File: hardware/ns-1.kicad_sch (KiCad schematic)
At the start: 66 parts, among them J6 Conn_01x11, J7 USB_C_Receptacle_USB2.0_16P, SW1 SW_Push_45deg, SW10 SW_Push_45deg, SW11 SW_Push_45deg, SW12 SW_Push_45deg, SW13 SW_Push_45deg, SW14 SW_Push_45deg, SW15 SW_Push_45deg, SW16 SW_Push_45deg, SW17 SW_Push_45deg, SW18 SW_Push_45deg, SW19 SW_Push_45deg, SW2 RotaryEncoder_Switch_MP, SW20 SW_Push, SW3 SW_Push_45deg, SW4 SW_Push_45deg, SW5 RotaryEncoder_Switch_MP, SW6 SW_Push_45deg, SW7 RotaryEncoder_Switch_MP, SW8 SW_Push_45deg, SW9 SW_Push_45deg, U1 Teensy4.1

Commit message: start respin to stm32h7
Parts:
- removed U1: Teensy4.1, footprints:Teensy41, symbol teensy:Teensy4.1
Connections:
- no-connect marks 27 -> 5
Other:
- added sheet STM32H7 (stm32h7.kicad_sch)
- added sheet teensy (teensy.kicad_sch)
- note added: "FerretCode"
- moved on the sheet: C2, C3, C4, C6, C8, R4, R5, R6, R7, R8, RV1, RV2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

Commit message: continue h7 revision
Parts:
- added R11, R12: 4.7k, symbol Device:R_Small_US
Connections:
- net +3.3V: now also R11.1, R12.1
- net SCL: now also R11.2
- net SDA: now also R12.2
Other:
- sheet Teensy Audio Shield renamed SGTL5000
- sheet SGTL5000: file teensy_audio_shield.kicad_sch -> sgtl5000.kicad_sch
- sheet SGTL5000 ports: added I2S_DIN, I2S_DOUT, I2S_LRCLK, I2S_SCLK, SYS_MCLK; removed BCLK, DIN, DOUT, LRCLK, MCLK
- sheet STM32H7 ports: added I2S_DIN, I2S_DOUT, I2S_LRCLK, I2S_SCLK, SCL, SDA, SYS_MCLK; removed none

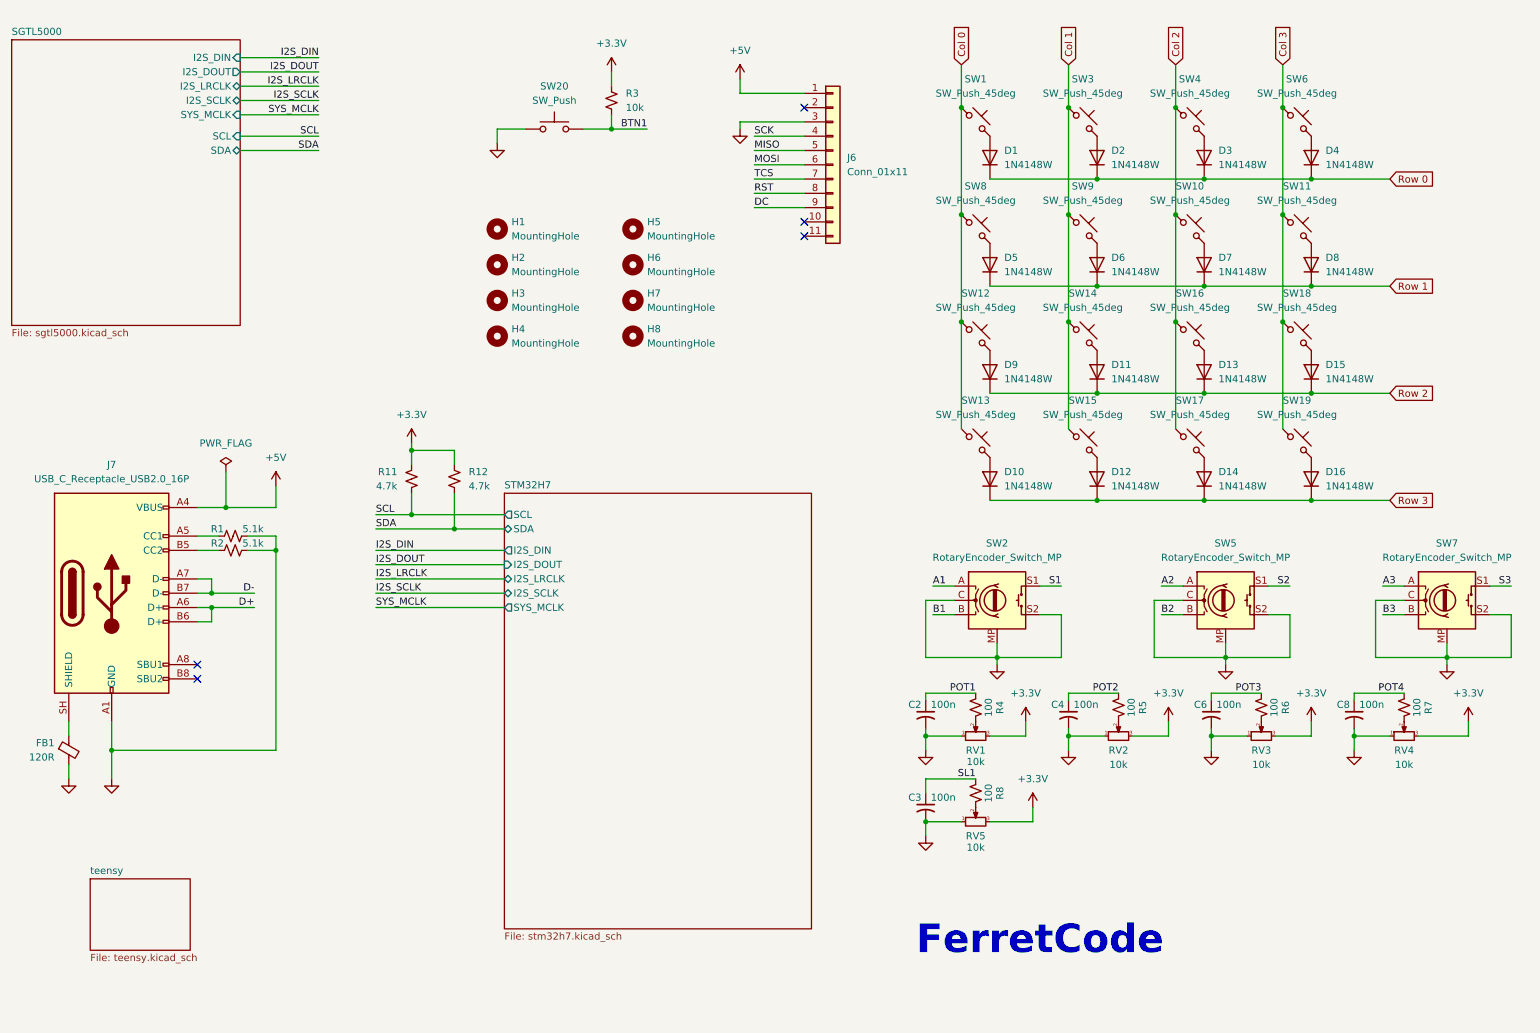
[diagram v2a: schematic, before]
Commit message: reorganize and finish codec / power
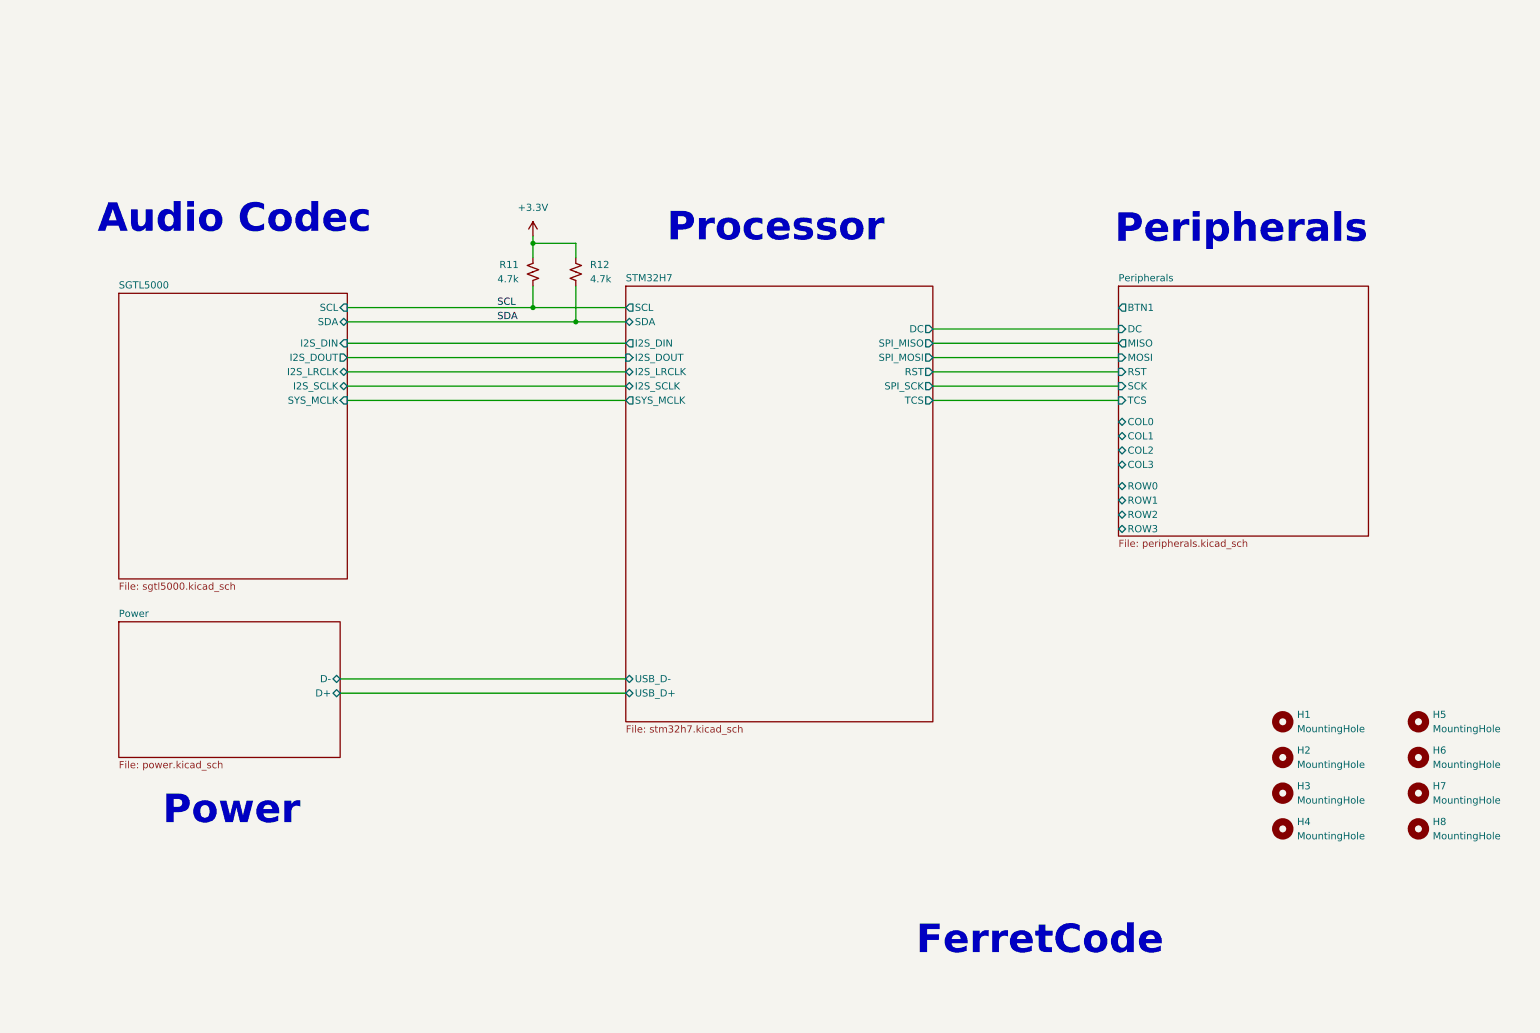
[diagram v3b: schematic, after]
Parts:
- removed C2, C3, C4, C6, C8: 100n, Capacitor_SMD:C_0402_1005Metric, symbol Device:C_Small_US
- removed D1, D10, D11, D12, D13, D14, D15, D16, D2, D3, D4, D5, D6, D7, D8, D9: 1N4148W, Diode_SMD:D_SOD-123, symbol Diode:1N4148W
- removed FB1: 120R, Inductor_SMD:L_0805_2012Metric, symbol Device:FerriteBead_Small
- removed J6: Conn_01x11, Connector_PinHeader_2.54mm:PinHeader_1x11_P2.54mm_Vertical, symbol Connector_Generic:Conn_01x11
- removed J7: USB_C_Receptacle_USB2.0_16P, Connector_USB:USB_C_Receptacle_HRO_TYPE-C-31-M-12, symbol Connector:USB_C_Receptacle_USB2.0_16P
- removed R1, R2: 5.1k, Resistor_SMD:R_0603_1608Metric, symbol Device:R_Small_US
- removed R3: 10k, Resistor_SMD:R_0603_1608Metric, symbol Device:R_Small_US
- removed R4, R5, R6, R7, R8: 100, Resistor_SMD:R_0603_1608Metric, symbol Device:R_Small_US
- removed RV1, RV2, RV3, RV4: 10k, Potentiometer_THT:Potentiometer_Alps_RK09K_Single_Vertical, symbol Device:R_Potentiometer_Small
- removed RV5: 10k, Potentiometer_THT:Potentiometer_Bourns_PTA4543_Single_Slide, symbol Device:R_Potentiometer_Small
- removed SW1, SW10, SW11, SW12, SW13, SW14, SW15, SW16, SW17, SW18, SW19, SW3, SW4, SW6, SW8, SW9: SW_Push_45deg, Button_Switch_Keyboard:SW_Cherry_MX_1.00u_PCB, symbol Switch:SW_Push_45deg
- removed SW2, SW5, SW7: RotaryEncoder_Switch_MP, Rotary_Encoder:RotaryEncoder_Alps_EC11E-Switch_Vertical_H20mm, symbol Device:RotaryEncoder_Switch_MP
- removed SW20: SW_Push, Button_Switch_Keyboard:SW_Cherry_MX_1.00u_PCB, symbol Switch:SW_Push
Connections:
- no-connect marks 5 -> 0
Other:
- removed sheet teensy
- added sheet Peripherals (peripherals.kicad_sch)
- added sheet Power (power.kicad_sch)
- sheet STM32H7 ports: added DC, RST, SPI_MISO, SPI_MOSI, SPI_SCK, TCS, USB_D+, USB_D-; removed none
- note added: "Audio Codec"
- note added: "Peripherals"
- note added: "Power"
- note added: "Processor"
- moved on the sheet: H1, H2, H3, H4, H5, H6, H7, H8, R11, R12

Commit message: start rearranging layout
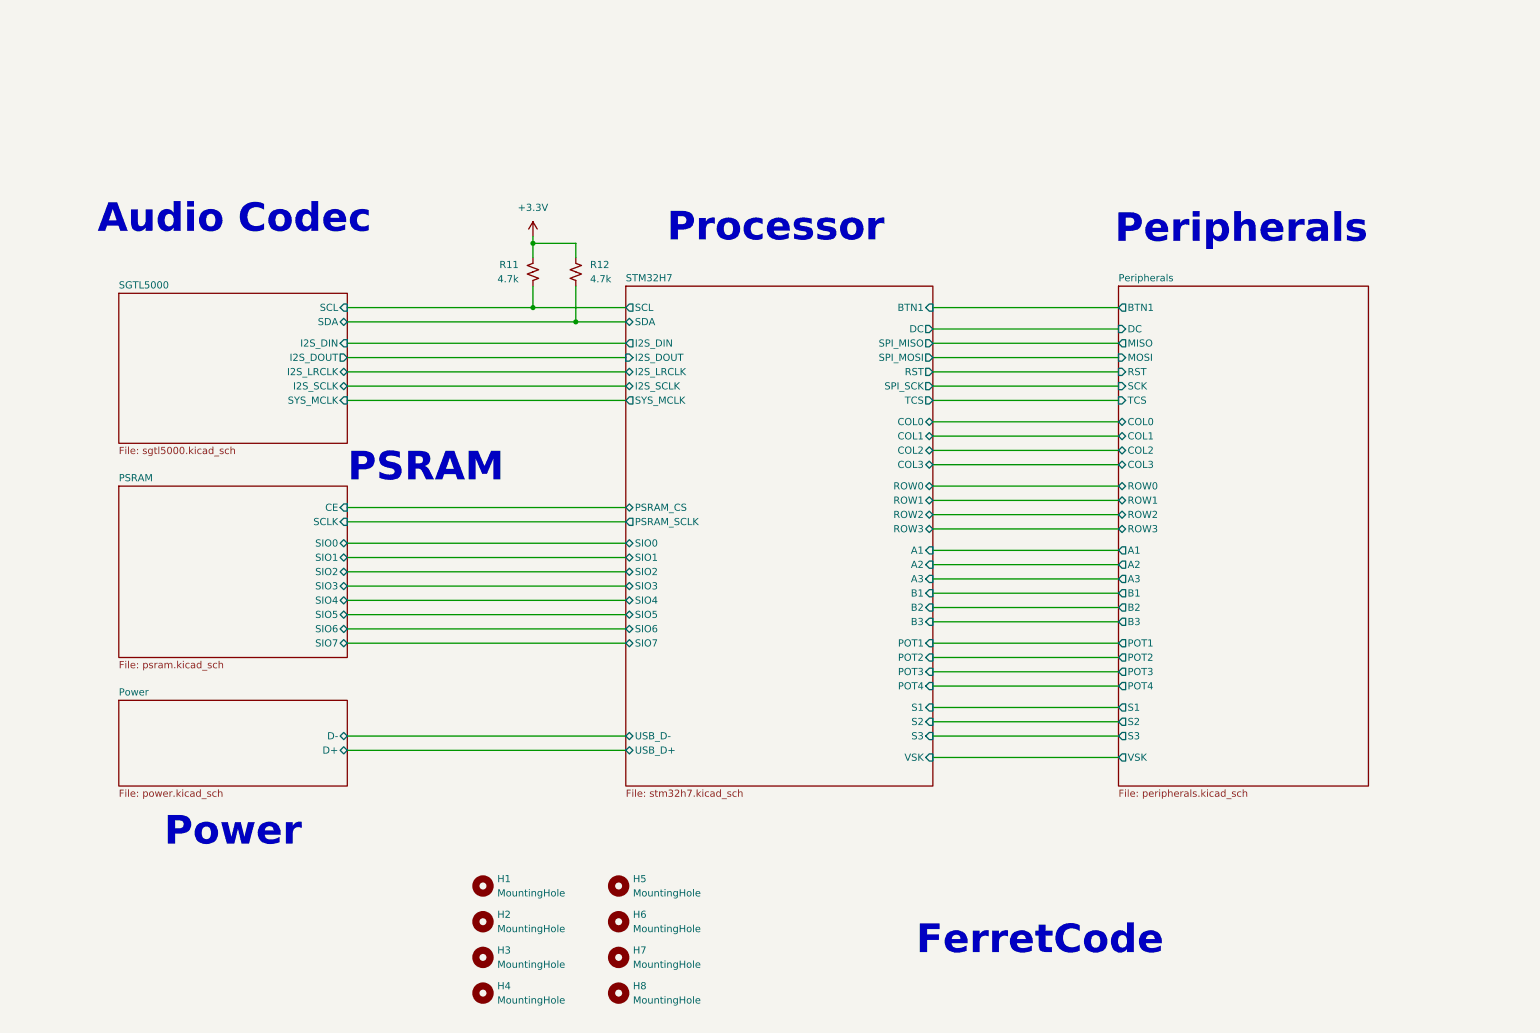
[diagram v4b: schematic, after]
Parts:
- R11, R12: footprint (none) -> Resistor_SMD:R_0402_1005Metric
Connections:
- net SCL renamed SGTL5000/SCL
- net SDA renamed SGTL5000/SDA
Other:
- added sheet PSRAM (psram.kicad_sch)
- sheet Peripherals ports: added A1, A2, A3, B1, B2, B3, POT1, POT2, POT3, POT4, S1, S2, S3, VSK; removed none
- sheet STM32H7 ports: added A1, A2, A3, B1, B2, B3, BTN1, COL0, COL1, COL2, COL3, POT1, POT2, POT3, POT4, PSRAM_CS, PSRAM_SCLK, ROW0, ROW1, ROW2, ROW3, S1, S2, S3, SIO0, SIO1, SIO2, SIO3, SIO4, SIO5, SIO6, SIO7, VSK; removed none
- note added: "PSRAM"
- moved on the sheet: H1, H2, H3, H4, H5, H6, H7, H8

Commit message: finish layout
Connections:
- net SGTL5000/SCL renamed SCL
- net SGTL5000/SDA renamed SDA
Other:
- sheet Peripherals ports: added SCL, SDA; removed none
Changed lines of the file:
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@@
+	)
+	(junction
+		(at 95.25 67.31)
+		(diameter 0)
+		(color 0 0 0 0)
+	)
+	(junction
+		(at 99.06 64.77)
+		(diameter 0)
+		(color 0 0 0 0)
 	)
 	(junction
@@
 	(wire
 		(pts
+			(xy 95.25 67.31) (xy 115.57 67.31)
+		)
+		(stroke
+			(width 0)
+			(type default)
+		)
+	)
+	(wire
+		(pts
 			(xy 179.07 101.6) (xy 212.09 101.6)
 		)
@@
 	(wire
 		(pts
+			(xy 82.55 57.15) (xy 95.25 57.15)
+		)
+		(stroke
+			(width 0)
+			(type default)
+		)
+	)
+	(wire
+		(pts
 			(xy 179.07 76.2) (xy 212.09 76.2)
 		)
@@
 	(wire
 		(pts
+			(xy 99.06 54.61) (xy 99.06 64.77)
+		)
+		(stroke
+			(width 0)
+			(type default)
+		)
+	)
+	(wire
+		(pts
 			(xy 74.93 140.97) (xy 124.46 140.97)
 		)
@@
 	(wire
 		(pts
-			(xy 74.93 67.31) (xy 115.57 67.31)
+			(xy 74.93 67.31) (xy 95.25 67.31)
 		)
 		(stroke
@@
 	(wire
 		(pts
-			(xy 74.93 64.77) (xy 107.95 64.77)
+			(xy 74.93 64.77) (xy 99.06 64.77)
 		)
 		(stroke
@@
 	(wire
 		(pts
+			(xy 256.54 67.31) (xy 266.7 67.31)
+		)
+		(stroke
+			(width 0)
+			(type default)
+		)
+	)
+	(wire
+		(pts
 			(xy 74.93 76.2) (xy 124.46 76.2)
 		)
@@
 	(wire
 		(pts
+			(xy 99.06 64.77) (xy 107.95 64.77)
+		)
+		(stroke
+			(width 0)
+			(type default)
+		)
+	)
+	(wire
+		(pts
+			(xy 95.25 57.15) (xy 95.25 67.31)
+		)
+		(stroke
+			(width 0)
+			(type default)
+		)
+	)
+	(wire
+		(pts
 			(xy 179.07 104.14) (xy 212.09 104.14)
 		)
@@
 	(wire
 		(pts
+			(xy 82.55 54.61) (xy 99.06 54.61)
+		)
+		(stroke
+			(width 0)
+			(type default)
+		)
+	)
+	(wire
+		(pts
 			(xy 74.93 78.74) (xy 124.46 78.74)
 		)
@@
 	(wire
 		(pts
+			(xy 256.54 64.77) (xy 266.7 64.77)
+		)
+		(stroke
+			(width 0)
+			(type default)
+		)
+	)
+	(wire
+		(pts
 			(xy 74.93 73.66) (xy 124.46 73.66)
 		)
@@
 			(width 0)
 			(type default)
+		)
+	)
+	(label "SCL"
+		(at 266.7 64.77 180)
+		(effects
+			(font
+				(size 1.27 1.27)
+			)
+			(justify right bottom)
+		)
+	)
+	(label "SDA"
+		(at 82.55 57.15 0)
+		(effects
+			(font
+				(size 1.27 1.27)
+			)
+			(justify left bottom)
+		)
+	)
+	(label "SDA"
+		(at 266.7 67.31 180)
+		(effects
+			(font
+				(size 1.27 1.27)
+			)
+			(justify right bottom)
+		)
+	)
+	(label "SCL"
+		(at 82.55 54.61 0)
+		(effects
+			(font
+				(size 1.27 1.27)
+			)
+			(justify left bottom)
 		)
 	)
@@
 			)
 		)
+		(pin "SCL" input
+			(at 256.54 64.77 0)
+			(effects
+				(font
+					(size 1.27 1.27)
+				)
+				(justify right)
+			)
+		)
+		(pin "SDA" bidirectional
+			(at 256.54 67.31 0)
+			(effects
+				(font
+					(size 1.27 1.27)
+				)
+				(justify right)
+			)
+		)

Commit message: finalize respin
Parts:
- R11, R12: LCSC PN (none) -> C25900
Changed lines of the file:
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@@
+			)
+		)
+		(property "LCSC PN" "C25900"
+			(at 115.57 58.42 0)
+			(hide yes)
+			(show_name no)
+			(do_not_autoplace no)
+			(effects
+				(font
+					(size 1.27 1.27)
+				)
 			)
 		)
@@
 			(at 107.95 58.42 0)
 			(hide yes)
+			(show_name no)
+			(do_not_autoplace no)
+			(effects
+				(font
+					(size 1.27 1.27)
+				)
+			)
+		)
+		(property "LCSC PN" "C25900"
+			(at 107.95 58.42 0)
+			(hide yes)
